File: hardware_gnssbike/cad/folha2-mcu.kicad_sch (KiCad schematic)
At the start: 7 parts, among them J201 Tag-Connect TC2030-NL, U201 MinewSemi ME54BS13

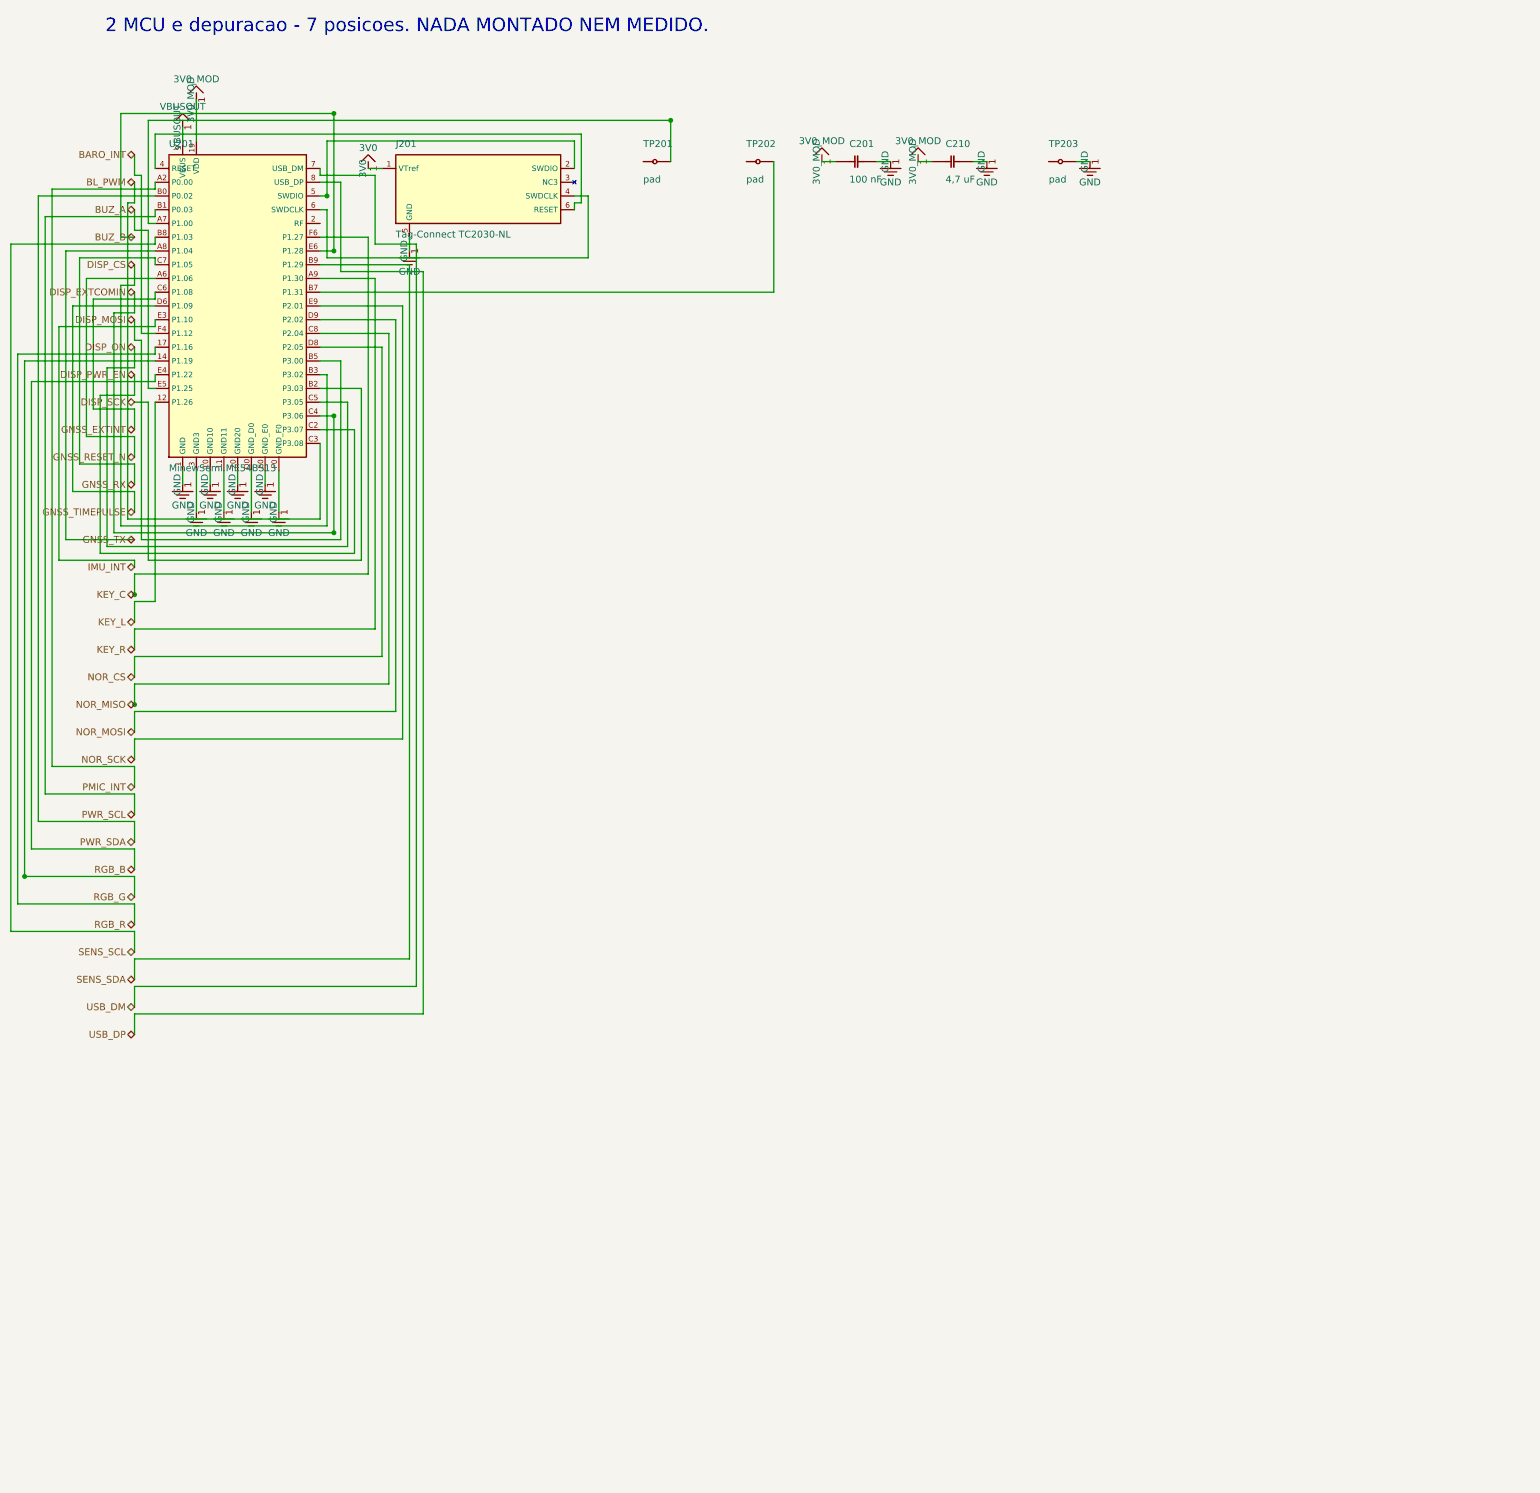
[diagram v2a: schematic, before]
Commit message: fix(hardware): the debug connector had RESET on the wrong contact
This one would have cost a board. The Tag-Connect TC2030 footprint had
pin 3 as no-connect and RESET on pin 6. The manufacturer's own data
sheet, TC2030-CTX_1.pdf, table "Connections", says the opposite: on the
six-pin footprint it is 3 = nRESET and 6 = SWO/TDO.

Where the mistake came from is worth writing down, because it is easy to
make twice: 1 VCC, 2 SWDIO, 3 GND, 4 SWCLK, 5 GND, 6 SWO is the
numbering of the ten-way Cortex header on the PROBE side, not of the
six-pin footprint on the board. Mixing the two gives exactly what was
written here.

What it would have done: the probe's nRESET is an open drain output, so
it would have driven nothing, and the MCU's reset would have hung off
the probe's SWO INPUT. Nothing burns - SWO runs target to probe, there
is no short - but the debugger can never reset the target: no connect
under reset, no pin reset. On an nRF54LM20A that reboots from task_wdt
or reconfigures its SWD pins, that removes the standard way out and
leaves only a full CTRL-AP erase.

The documentation carried a worse version still. 06 had GND on contact 3,
which fabricated would tie the probe's open-drain nRESET to copper
ground and hold the target in reset forever.

The project's own notes had predicted this exact variant - 06 carried a
CAUTION saying so and README an open checklist item. It was that one, and
it was caught before layout. Both are now closed, and the connector's
pin 6 is recorded as SWO with what is still unknown about it: which pad
of the ME54BS13 exposes SWO, which would give printf over ITM during
bring-up.

Fixed in parts.py, nets.py, 03-netlist.md, 06-conectores-e-pontos-de-teste.md,
07-sequencias-e-protecao.md and README.md.

Verified: check_sch and check_pcb pass, 78 of 78 diagrams render, 1529
links and none broken.
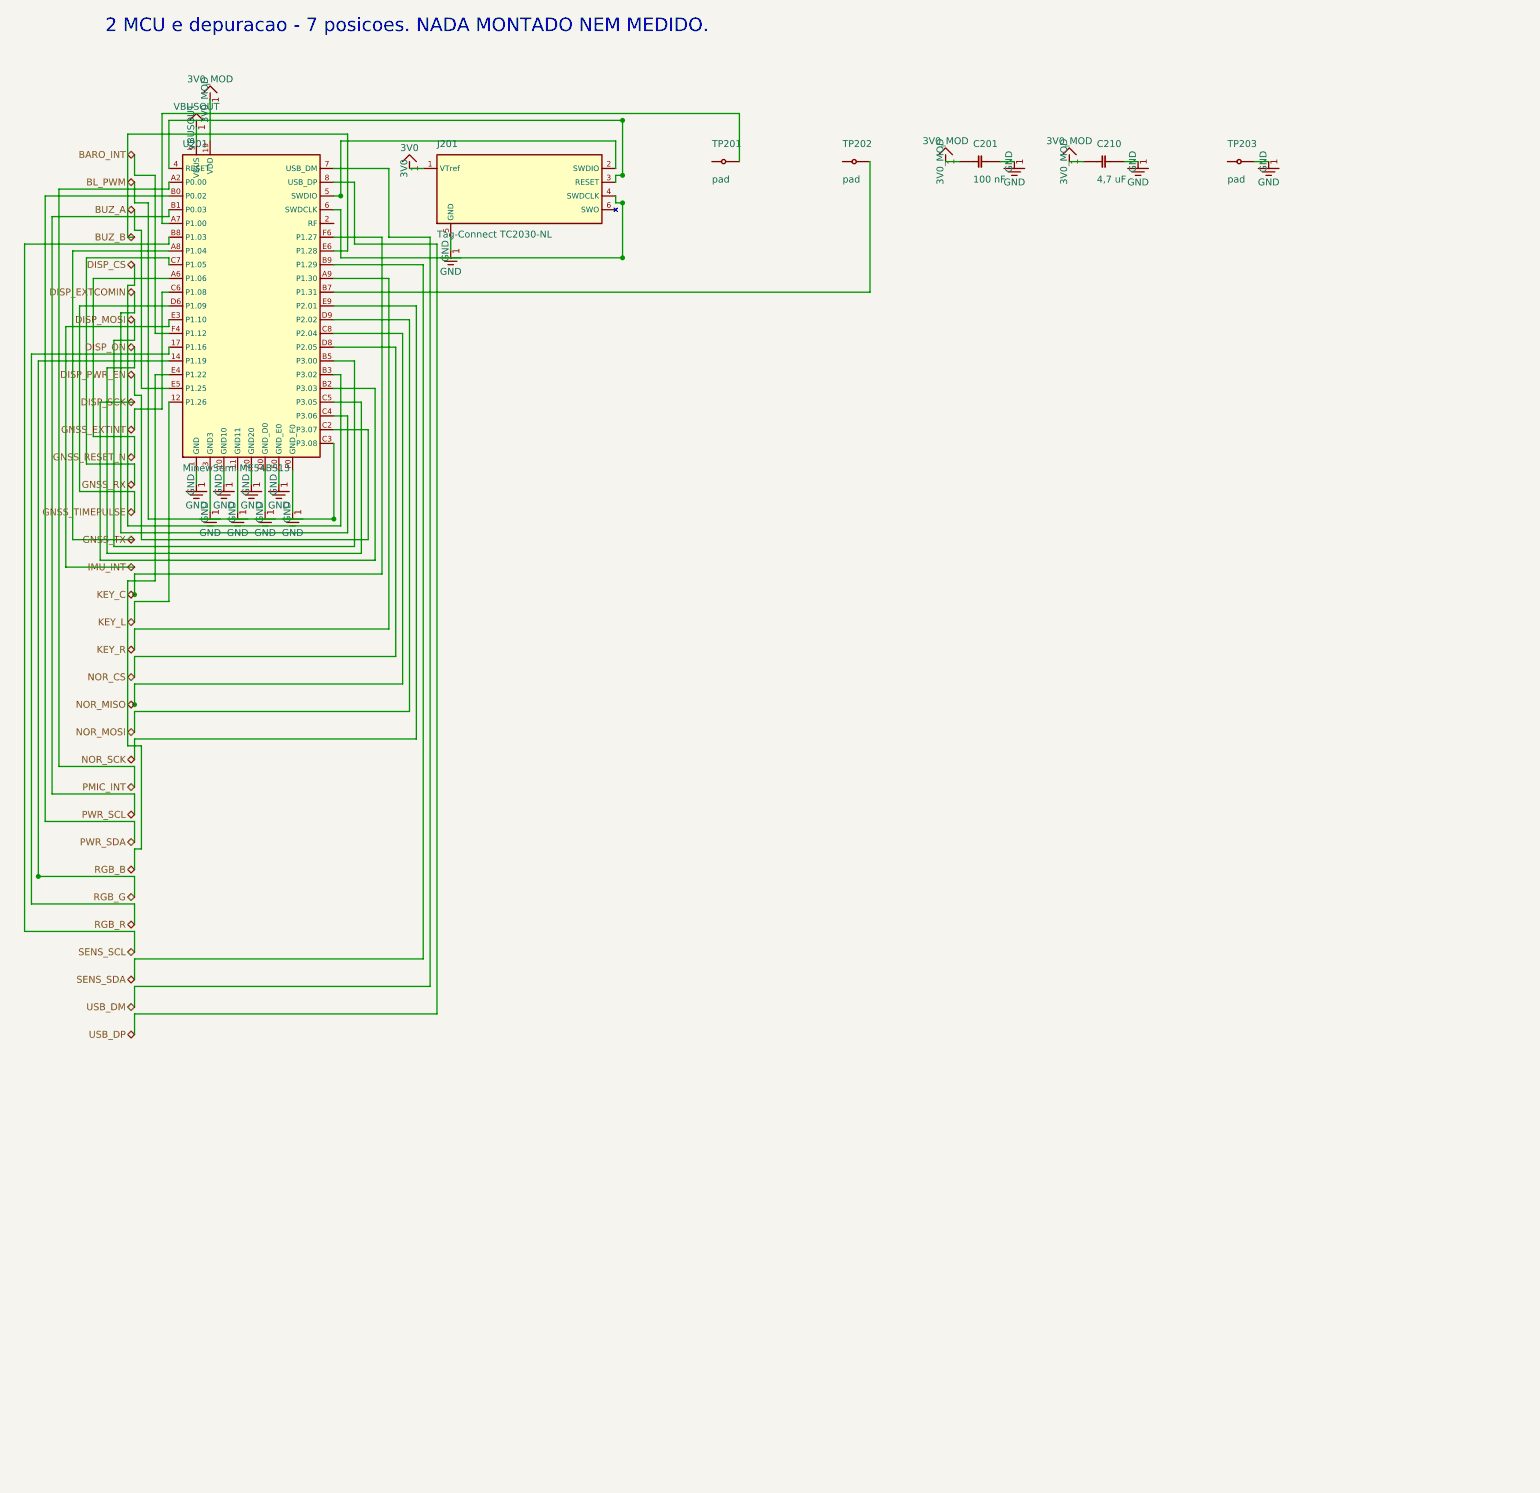
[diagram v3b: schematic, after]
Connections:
- net at U201.4 (RESET): now also J201.3 (RESET); no longer J201.6 (RESET)
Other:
- moved on the sheet: C201, C210, J201, TP201, TP202, TP203, U201

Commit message: feat(hardware): the ERC runs, and 52 hidden errors became 4 deliberate ones
check_sch.py compared our netlist against the one KiCad extracts, pin by
pin, and was good at that and blind to everything else. KiCad's own ERC
had never been run on this schematic. It found 52 errors, and among them
a capacitor with BOTH terminals in the air.

They were of four kinds, and three of them were the drawing failing to
say what it meant rather than the circuit being wrong:

  34 open pins with no flag. The NC pins of the ESD array, the GPIOs
  nobody uses, the receiver's SDA and SCL - it speaks UART - the
  programmer's SWO. Every one of them deliberate, and indistinguishable
  from a forgotten wire. They now carry a no-connect flag, taken from
  nets.py, which is already the source of truth about what is open: a
  pin that appears in no net is open, full stop. A net with a single pin
  counts as open too, which is what R111 became when the harvester
  changed and its pull-up lost its job.

  12 rails with no source the ERC could see. The 1V8_GNSS comes from
  1V8 through a ferrite, the SD3V0_FLASH from SD3V0 through a jumper,
  the harvester's VIN from the panel. PWR_FLAG is the symbol that exists
  to say "this is supplied, I answer for it". One per ELECTRICAL GROUP,
  not per net and not per sheet: two nets that share a pin are one net
  to KiCad - the display connector carries FPC_VSS on one side and GND
  on the other through the same contact - and a flag on each side would
  be two supply outputs wired together, which is another error.

  The last one needed the electrical type to come from the symbol that
  actually reaches the sheet. The four VBUS contacts of the USB-C are
  power_out in our parts.py and passive in KiCad's symbol, so the rule
  believed the rail had a source when it had none.

What is left is four violations, and all four are the same thing: two
supply OUTPUTS wired together. KiCad calls that an error by default
because in signal circuitry two outputs on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
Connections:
- no-connect marks 0 -> 2
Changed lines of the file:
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@@
 		(stroke (width 0) (type default))
+	)
+	(no_connect
+		(at 62.230 46.990)
+	)
+	(no_connect
+		(at 114.300 44.450)
 	)
 	(junction
